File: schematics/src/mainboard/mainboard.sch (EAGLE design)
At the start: 65 parts, among them IC1 LM324N, IC2 7805T, IC3 UA741P, IC6 LM324N, IC8 CA3080E, Q1 BC550C, Q2 BC550C, Q3 BC550C

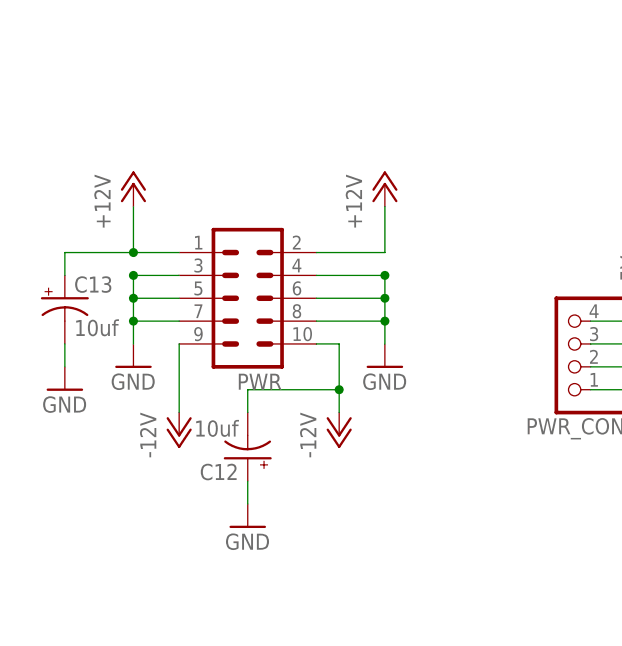
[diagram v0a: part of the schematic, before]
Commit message: Updated Schematics, Fixed Power Socket orientation
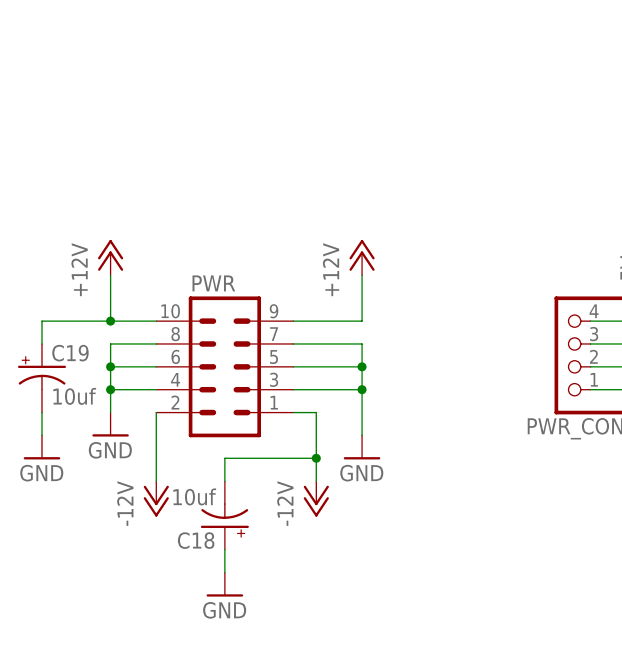
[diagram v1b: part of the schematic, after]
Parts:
- removed C12, C13: 10uf, resistor:CPOL-USE2.5-5
- added C18, C19: 10uf, resistor:CPOL-USE2.5-5
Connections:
- net +12V: now also C19.+, PWR.10, PWR.9; no longer C13.+, PWR.1, PWR.2
- net -12V: now also C18.-, PWR.1, PWR.2; no longer C12.-, PWR.10, PWR.9
- net GND: now also C18.+, C19.-; no longer C12.+, C13.-
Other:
- moved on the sheet: PWR

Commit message: Fixed some bugs and updated documentation
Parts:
- C8: value 47nF/16v -> 47nF; device rcl:CPOL-USE2.5-6 -> rcl:C-EU050-024X044
- R31: value 33k -> 22k
- R32: value 10k -> 100k
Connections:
- net N$17: now also C8.2; no longer C8.-
- net N$18: now also C8.1; no longer C8.+
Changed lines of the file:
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@@
 <part name="R17" library="rcl" library_urn="urn:adsk.eagle:library:334" deviceset="R-US_" device="0207/7" package3d_urn="urn:adsk.eagle:package:23493/2" value="470k"/>
 <part name="C7" library="rcl" library_urn="urn:adsk.eagle:library:334" deviceset="C-EU" device="050-024X044" package3d_urn="urn:adsk.eagle:package:23643/1" value="22pF"/>
-<part name="C8" library="rcl" library_urn="urn:adsk.eagle:library:334" deviceset="CPOL-US" device="E2.5-6" package3d_urn="urn:adsk.eagle:package:23349/1" value="47nF/16v"/>
+<part name="C8" library="rcl" library_urn="urn:adsk.eagle:library:334" deviceset="C-EU" device="050-024X044" package3d_urn="urn:adsk.eagle:package:23643/1" value="47nF"/>
 <part name="R18" library="rcl" library_urn="urn:adsk.eagle:library:334" deviceset="R-US_" device="0207/7" package3d_urn="urn:adsk.eagle:package:23493/2" value="10k"/>
 <part name="R19" library="rcl" library_urn="urn:adsk.eagle:library:334" deviceset="R-US_" device="0207/7" package3d_urn="urn:adsk.eagle:package:23493/2" value="100k"/>
@@
 <part name="R30" library="rcl" library_urn="urn:adsk.eagle:library:334" deviceset="R-US_" device="0207/7" package3d_urn="urn:adsk.eagle:package:23493/2" value="47k"/>
 <part name="C11" library="rcl" library_urn="urn:adsk.eagle:library:334" deviceset="CPOL-US" device="E2.5-6" package3d_urn="urn:adsk.eagle:package:23349/1" value="1uF/16v"/>
-<part name="R31" library="rcl" library_urn="urn:adsk.eagle:library:334" deviceset="R-US_" device="0207/7" package3d_urn="urn:adsk.eagle:package:23493/2" value="33k"/>
-<part name="R32" library="rcl" library_urn="urn:adsk.eagle:library:334" deviceset="R-US_" device="0207/7" package3d_urn="urn:adsk.eagle:package:23493/2" value="10k"/>
+<part name="R31" library="rcl" library_urn="urn:adsk.eagle:library:334" deviceset="R-US_" device="0207/7" package3d_urn="urn:adsk.eagle:package:23493/2" value="22k"/>
+<part name="R32" library="rcl" library_urn="urn:adsk.eagle:library:334" deviceset="R-US_" device="0207/7" package3d_urn="urn:adsk.eagle:package:23493/2" value="100k"/>
 <part name="P+4" library="supply1" library_urn="urn:adsk.eagle:library:371" deviceset="+12V" device=""/>
 <part name="P-1" library="supply1" library_urn="urn:adsk.eagle:library:371" deviceset="-12V" device=""/>
@@
 <wire x1="162.56" y1="106.68" x2="167.64" y2="106.68" width="0.1524" layer="91"/>
 <junction x="162.56" y="106.68"/>
-<pinref part="C8" gate="G$1" pin="+"/>
+<pinref part="C8" gate="G$1" pin="1"/>
 </segment>
 </net>
 <net name="N$17" class="0">
 <segment>
-<pinref part="C8" gate="G$1" pin="-"/>
+<pinref part="C8" gate="G$1" pin="2"/>
 <pinref part="R18" gate="G$1" pin="2"/>
 <wire x1="177.8" y1="106.68" x2="175.26" y2="106.68" width="0.1524" layer="91"/>
